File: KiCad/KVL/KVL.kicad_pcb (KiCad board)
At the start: 2 copper layers, 279.5 x 95 mm, 251 parts, among them J1 AudioJack2_Ground, J2 Conn_01x04, J3 AudioJack2_Ground, J4 Conn_01x11, SW1 SW_MEC_5G, SW10 SW_MEC_5G, SW11 SW_MEC_5G, SW12 SW_MEC_5G, SW13 SW_MEC_5G, SW14 SW_MEC_5G, SW15 SW_MEC_5G, SW16 SW_MEC_5G, SW17 SW_MEC_5G, SW18 SW_MEC_5G, SW19 SW_MEC_5G, SW2 SW_MEC_5G, SW20 SW_MEC_5G, SW21 SW_MEC_5G, SW22 SW_MEC_5G, SW23 SW_MEC_5G, SW24 SW_MEC_5G, SW25 SW_MEC_5G, SW26 SW_MEC_5G, SW27 SW_MEC_5G, SW28 SW_MEC_5G, SW29 SW_MEC_5G, SW3 SW_MEC_5G, SW30 SW_MEC_5G, SW31 SW_MEC_5G, SW32 SW_MEC_5G, SW33 SW_MEC_5G, SW34 SW_MEC_5G, SW35 SW_MEC_5G, SW36 SW_MEC_5G, SW37 SW_MEC_5G, SW38 SW_MEC_5G, SW39 SW_MEC_5G, SW4 SW_MEC_5G, SW40 SW_MEC_5G, SW41 SW_MEC_5G, SW42 SW_MEC_5G, SW43 SW_MEC_5G, SW44 SW_MEC_5G, SW45 SW_MEC_5G, SW46 SW_MEC_5G, SW47 SW_MEC_5G, SW48 SW_MEC_5G, SW49 SW_MEC_5G, SW5 SW_MEC_5G, SW50 SW_MEC_5G, SW51 SW_MEC_5G, SW52 SW_MEC_5G, SW53 SW_MEC_5G, SW54 SW_MEC_5G, SW55 SW_MEC_5G, SW56 SW_MEC_5G, SW57 SW_MEC_5G, SW58 SW_MEC_5G, SW59 SW_MEC_5G, SW6 SW_MEC_5G, SW60 SW_MEC_5G, SW61 SW_MEC_5G, SW62 SW_MEC_5G, SW63 SW_MEC_5G, SW64 SW_MEC_5G, SW65 SW_MEC_5G, SW7 SW_MEC_5G, SW8 SW_MEC_5G, SW9 SW_MEC_5G, U1 74HC164, U2 74HC165, U3 74HC165, U5 ADAU1761BCPZ, U6 MIC2005A-1YM5-TR

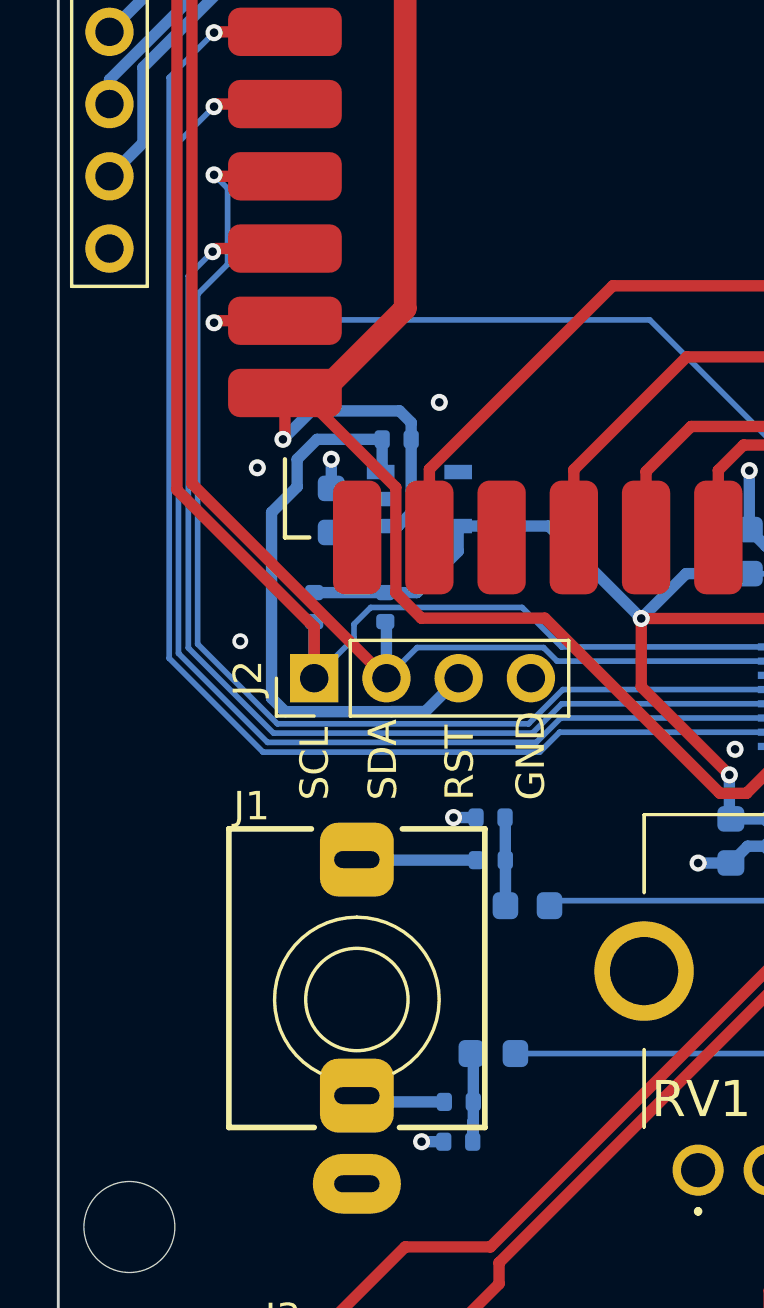
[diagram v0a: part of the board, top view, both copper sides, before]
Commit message: Added Line/Phono Switching LED.
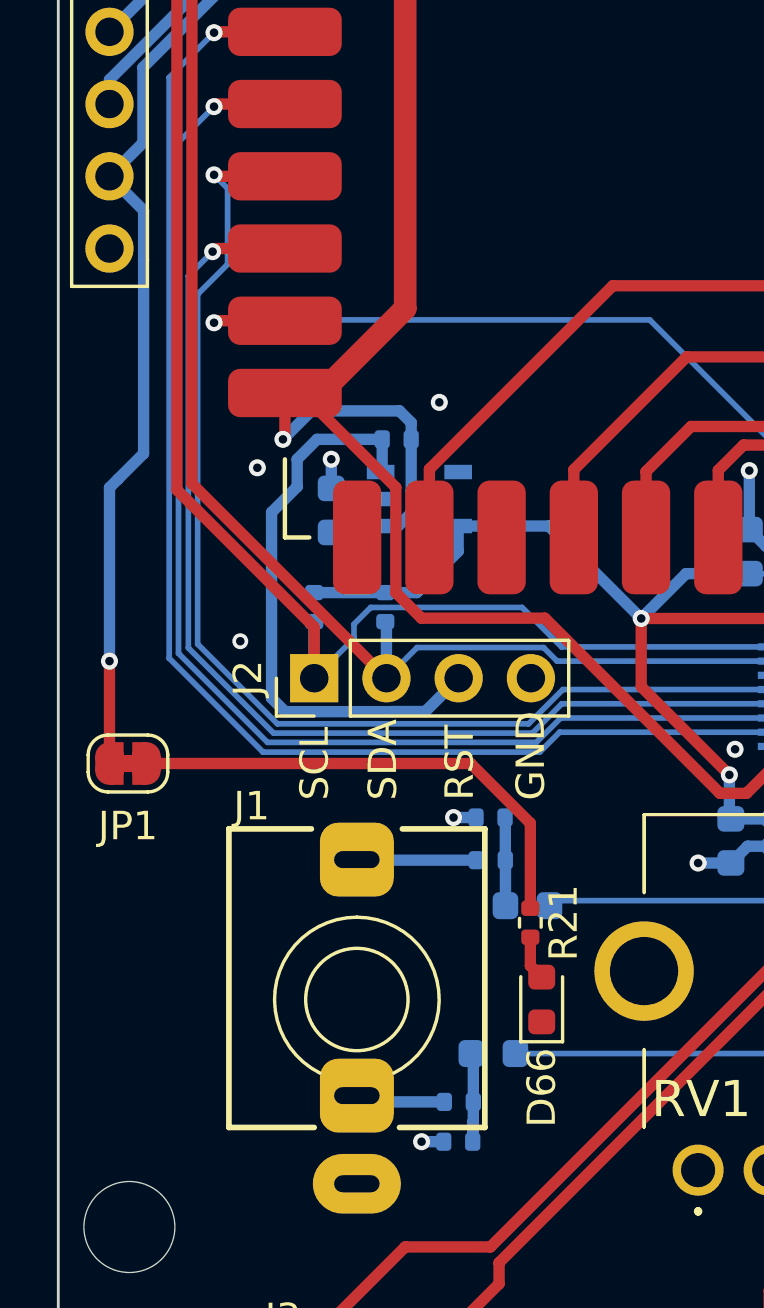
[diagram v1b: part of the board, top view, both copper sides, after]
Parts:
- added D66: LED, LED_SMD:LED_0603_1608Metric, F.Cu at (75.5, 157.0)
- added JP1: Jumper_2_Bridged, Jumper:SolderJumper-2_P1.3mm_Bridged_RoundedPad1.0x1.5mm, F.Cu at (61.0, 148.7)
- added R21: 1k, Resistor_SMD:R_0402_1005Metric, F.Cu at (75.1, 154.3)
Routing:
- net /ICs/PB2: track 40.9 -> 62.5 mm, vias 1 -> 2
- net Net-(JP1-B): track 0.00 -> 17.4 mm
- net Net-(D66-A): track 0.00 -> 1.57 mm
